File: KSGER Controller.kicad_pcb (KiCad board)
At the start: 2 copper layers, 114.3 x 40.6 mm, 51 parts, among them J1 24 VDC, J2 IRON_IN, J4 BATT, Q1 IRF7416, Q2 S8050, SW1 ENCODER, U1 STM32F103C8Tx, U2 AMS1117-3.3, U3 SGM8551, U4 24LC08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

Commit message: Playing with trace widths
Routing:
- net +3V3: track 274.2 -> 273.4 mm

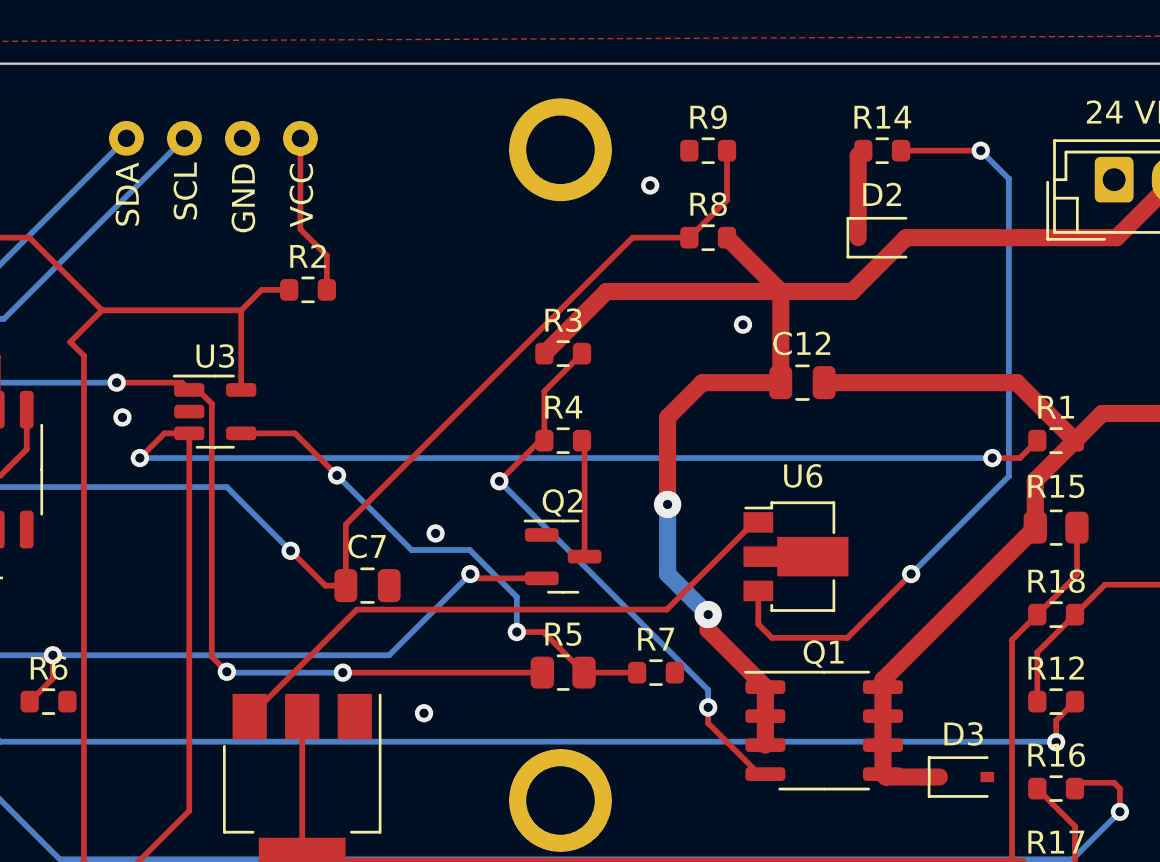
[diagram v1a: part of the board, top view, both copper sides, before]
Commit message: Adjusting traces again
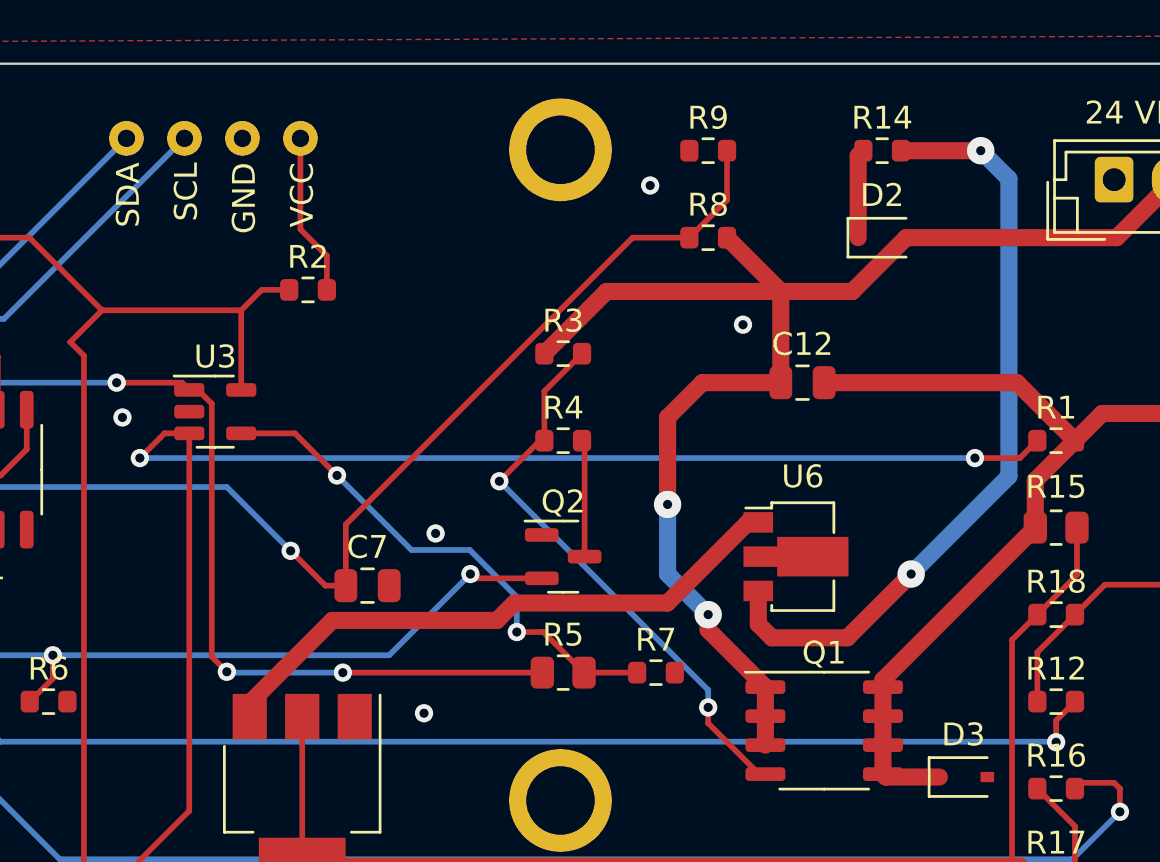
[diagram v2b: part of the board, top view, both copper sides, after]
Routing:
- net Net-(U2-Pad3): track 25.8 -> 26.3 mm
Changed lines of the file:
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@@
   (segment (start 146.1825 93.66) (end 145.1 93.66) (width 0.25) (layer "F.Cu") (net 10))
   (segment (start 146.1825 110.195) (end 146.1825 93.66) (width 0.25) (layer "F.Cu") (net 10))
-  (segment (start 181.356 94.742) (end 182.563 94.742) (width 0.25) (layer "F.Cu") (net 10))
+  (segment (start 180.594 94.742) (end 182.563 94.742) (width 0.25) (layer "F.Cu") (net 10))
   (segment (start 182.563 94.742) (end 183.325 93.98) (width 0.25) (layer "F.Cu") (net 10))
   (segment (start 145.1 93.66) (end 144.018 94.742) (width 0.25) (layer "F.Cu") (net 10))
   (segment (start 140.8075 115.57) (end 146.1825 110.195) (width 0.25) (layer "F.Cu") (net 10))
-  (via (at 181.356 94.742) (size 0.8) (drill 0.4) (layers "F.Cu" "B.Cu") (net 10))
+  (via (at 180.594 94.742) (size 0.8) (drill 0.4) (layers "F.Cu" "B.Cu") (net 10))
   (via (at 144.018 94.742) (size 0.8) (drill 0.4) (layers "F.Cu" "B.Cu") (net 10))
-  (segment (start 144.018 94.742) (end 181.356 94.742) (width 0.25) (layer "B.Cu") (net 10))
+  (segment (start 144.018 94.742) (end 180.594 94.742) (width 0.25) (layer "B.Cu") (net 10))
   (segment (start 175.48 81.505) (end 175.48 85.09) (width 0.75) (layer "F.Cu") (net 11))
   (segment (start 175.705 81.28) (end 175.48 81.505) (width 0.75) (layer "F.Cu") (net 11))
@@
   (segment (start 184.127489 107.165489) (end 184.15 107.188) (width 0.25) (layer "B.Cu") (net 25))
   (segment (start 130.048 99.314) (end 137.899489 107.165489) (width 0.25) (layer "B.Cu") (net 25))
-  (segment (start 171.704 102.616) (end 175.006 102.616) (width 0.25) (layer "F.Cu") (net 26))
-  (segment (start 171.105 102.017) (end 171.704 102.616) (width 0.25) (layer "F.Cu") (net 26))
-  (segment (start 175.006 102.616) (end 177.8 99.822) (width 0.25) (layer "F.Cu") (net 26))
-  (segment (start 180.848 81.28) (end 177.355 81.28) (width 0.25) (layer "F.Cu") (net 26))
-  (segment (start 171.105 100.56) (end 171.105 102.017) (width 0.25) (layer "F.Cu") (net 26))
-  (via (at 180.848 81.28) (size 0.8) (drill 0.4) (layers "F.Cu" "B.Cu") (net 26))
-  (via (at 177.8 99.822) (size 0.8) (drill 0.4) (layers "F.Cu" "B.Cu") (net 26))
-  (segment (start 182.080511 82.512511) (end 180.848 81.28) (width 0.25) (layer "B.Cu") (net 26))
-  (segment (start 177.8 99.822) (end 182.080511 95.541489) (width 0.25) (layer "B.Cu") (net 26))
-  (segment (start 182.080511 95.541489) (end 182.080511 82.512511) (width 0.25) (layer "B.Cu") (net 26))
+  (segment (start 171.704 102.616) (end 175.006 102.616) (width 0.75) (layer "F.Cu") (net 26))
+  (segment (start 171.105 102.017) (end 171.704 102.616) (width 0.75) (layer "F.Cu") (net 26))
+  (segment (start 175.006 102.616) (end 177.8 99.822) (width 0.75) (layer "F.Cu") (net 26))
+  (segment (start 180.848 81.28) (end 177.355 81.28) (width 0.75) (layer "F.Cu") (net 26))
+  (segment (start 171.105 100.56) (end 171.105 102.017) (width 0.75) (layer "F.Cu") (net 26))
+  (via (at 180.848 81.28) (size 1.2) (drill 0.4) (layers "F.Cu" "B.Cu") (net 26))
+  (via (at 177.8 99.822) (size 1.2) (drill 0.4) (layers "F.Cu" "B.Cu") (net 26))
+  (segment (start 182.080511 82.512511) (end 180.848 81.28) (width 0.75) (layer "B.Cu") (net 26))
+  (segment (start 177.8 99.822) (end 182.080511 95.541489) (width 0.75) (layer "B.Cu") (net 26))
+  (segment (start 182.080511 95.541489) (end 182.080511 82.512511) (width 0.75) (layer "B.Cu") (net 26))
   (segment (start 124.8125 96.5) (end 125.972614 96.5) (width 0.25) (layer "F.Cu") (net 27))
   (segment (start 186.69 108.966) (end 185.229 108.966) (width 0.25) (layer "F.Cu") (net 27))
@@
   (segment (start 122.936 88.646) (end 122.682 88.9) (width 0.25) (layer "B.Cu") (net 38))
   (segment (start 145.9715 80.74) (end 138.0655 88.646) (width 0.25) (layer "B.Cu") (net 38))
+  (segment (start 170.655489 97.56) (end 171.105 97.56) (width 0.75) (layer "F.Cu") (net 51))
   (segment (start 170.918 97.56) (end 171.105 97.56) (width 0.25) (layer "F.Cu") (net 51))
-  (segment (start 167.09848 101.37952) (end 170.918 97.56) (width 0.25) (layer "F.Cu") (net 51))
-  (segment (start 148.83 106.07) (end 153.52048 101.37952) (width 0.25) (layer "F.Cu") (net 51))
-  (segment (start 153.52048 101.37952) (end 167.09848 101.37952) (width 0.25) (layer "F.Cu") (net 51))
+  (segment (start 148.83 106.07) (end 148.83 105.470978) (width 0.75) (layer "F.Cu") (net 51))
+  (segment (start 167.123489 101.092) (end 170.655489 97.56) (width 0.75) (layer "F.Cu") (net 51))
+  (segment (start 159.657832 101.854) (end 160.419832 101.092) (width 0.75) (layer "F.Cu") (net 51))
+  (segment (start 160.419832 101.092) (end 167.123489 101.092) (width 0.75) (layer "F.Cu") (net 51))
+  (segment (start 152.446978 101.854) (end 159.657832 101.854) (width 0.75) (layer "F.Cu") (net 51))
+  (segment (start 148.83 105.470978) (end 152.446978 101.854) (width 0.75) (layer "F.Cu") (net 51))
   (zone (net 4) (net_name "GND") (layer "F.Cu") (name "Ground Fill") (hatch edge 0.508)
     (connect_pads (clearance 0.508))
